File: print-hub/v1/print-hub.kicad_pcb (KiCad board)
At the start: 4 copper layers, 104 x 66 mm, 136 parts, among them J1 USB-C, J101 USB-A, J2 USB-C, J201 USB-A, J301 USB-A, J401 USB-A, J501 USB-A, SW1 button, SW2 button, U1 HUSB238, U101 TPS25200, U102 INA180A2, U2 SY8368A, U201 TPS25200, U202 INA180A2, U3 USBLC6-2SC6, U301 TPS25200, U302 INA180A2, U4 AP2112K-3.3, U401 TPS25200, U402 INA180A2, U5 ESP32-S3-WROOM-1-N8, U501 TPS25200, U502 INA180A2

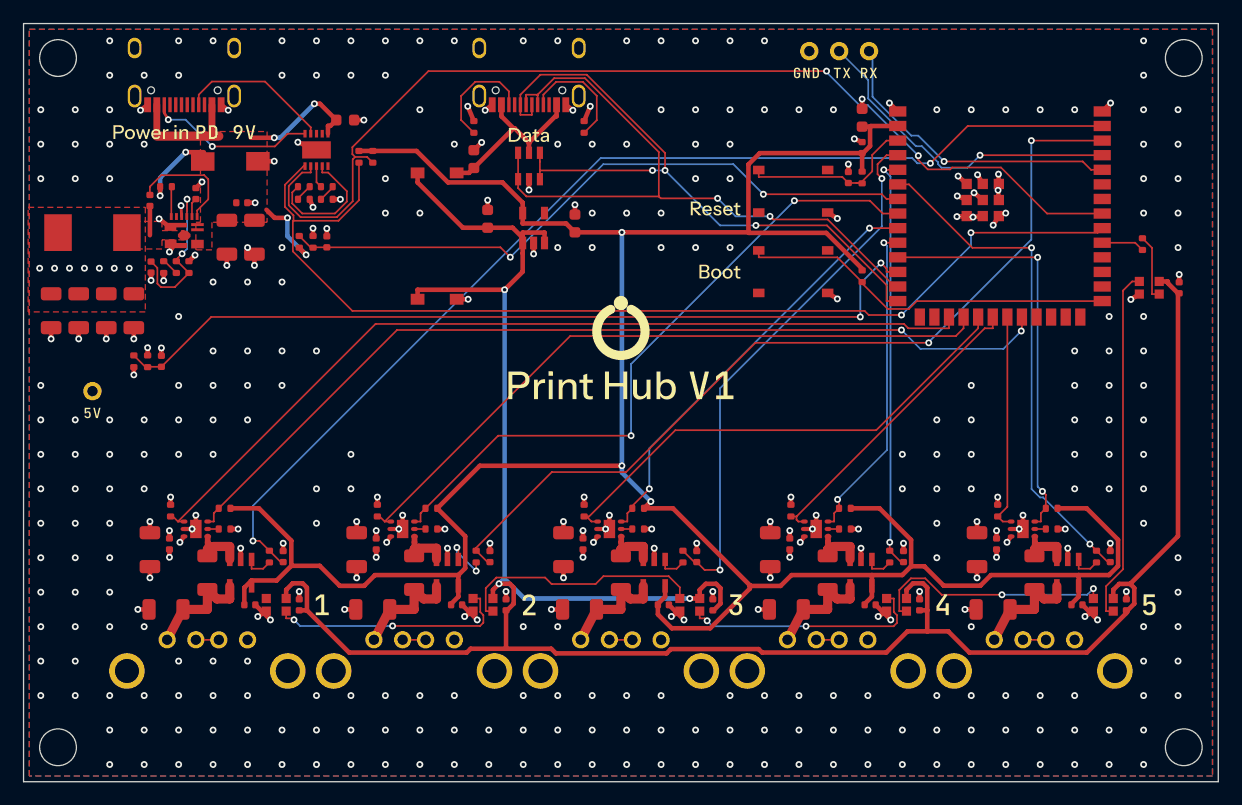
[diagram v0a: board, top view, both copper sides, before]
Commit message: print-hub v1: 86 x 50 mm board, 45-degree corners, heat simulation and protection
- Board shrunk from 104 x 66 to 86 x 50 mm (under JLCPCB's 100 mm price
  break: $8 for five 4-layer boards instead of $29); ports 17 mm apart,
  two M3 holes; green mask, lead-free HASL (cheapest build).
- src/miter.py cuts every track corner to 45 degrees after routing; a
  build gate checks it. Port power tracks drawn with 45-degree bends.
- sim/thermal/board_heat.py: the routed board's heat in its PETG case
  (solver from ridge3-lite). Total output capped at 3 A; a thermistor
  (NTC on GPIO9; port 1's enable moves to GPIO21) lets the firmware turn
  ports down when hot.
- Firmware 1.1.0: heat protection, 3 A budget, 80 MHz CPU; CLI and web
  page show the board temperature. docs/home-assistant.md.
- Enclosure update to follow.

Co-Authored-By: Claude Opus 5.5 <noreply@anthropic.com>
Claude-Session: https://claude.ai/code/session_01AiCo3BFL3vgJ9qSJmY4RFn
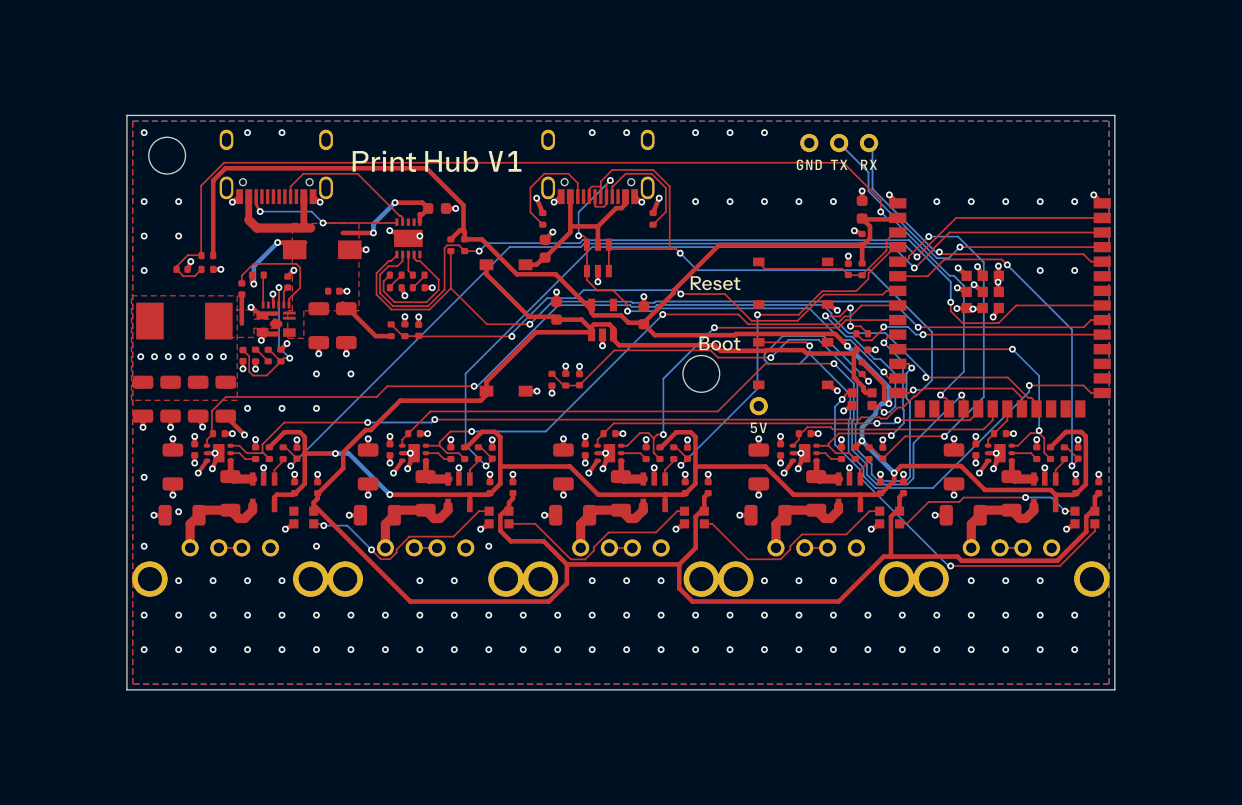
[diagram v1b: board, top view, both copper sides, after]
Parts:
- removed the C11 at (57.6, 92.0)
- removed H3, H4: HOLE, MOUNT_M3
- removed the R10 at (62.4, 88.2)
- added C21: 100nF, C_0402_1005Metric, F.Cu at (121.0, 95.4)
- added C7: 100nF, C_0402_1005Metric, F.Cu at (61.8, 88.4)
- added R12: 10k, R_0402_1005Metric, F.Cu at (70.4, 95.9)
- added R20: 10k, R_0402_1005Metric, F.Cu at (121.0, 97.0)
- added R21: 100R, R_0402_1005Metric, F.Cu at (121.0, 94.0)
- C11: renamed from R12; value 15k -> 22uF; footprint R_0402_1005Metric -> C_1206_3216Metric
- C12: value 100nF -> 22uF; footprint C_0402_1005Metric -> C_1206_3216Metric
- C14: value 10uF -> 100nF; footprint C_0603_1608Metric -> C_0402_1005Metric
- C17: value 22uF -> 10uF
- C18: value 100nF -> 22uF; footprint C_0402_1005Metric -> C_0603_1608Metric
- C19: value 1uF -> 100nF
- C20: value 100nF -> 1uF
- C8: value 22uF -> 22pF; footprint C_1206_3216Metric -> C_0402_1005Metric
- R10: renamed from C7; value 22pF -> 75k; footprint C_0402_1005Metric -> R_0402_1005Metric
- R11: value 100k -> 1k
- R14: value 100k -> 15k
- R15, R16: value 5.1k -> 100k
- R17, R18: value 10k -> 5.1k
- R19: value 100R -> 10k
- R8: value 75k -> 10k NTC
- R9: value 1k -> 10k
- moved TP4 58.0 mm to (112.0, 100.3)
- moved H2 50.2 mm to (107.0, 97.5)
- moved C20 28.8 mm to (119.8, 88.4)
- moved R18 28.2 mm to (93.2, 84.0)
- moved LED1 26.8 mm to (121.0, 99.7)
- moved C17 25.6 mm to (102.0, 92.4)
- moved R19 24.5 mm to (121.0, 88.4)
- moved R16 23.4 mm to (95.2, 98.0)
- moved C13 22.6 mm to (82.4, 93.7)
- moved R14 22.6 mm to (81.2, 93.7)
- moved R13 22.6 mm to (80.0, 93.7)
- moved R15 22.2 mm to (94.0, 98.0)
- moved C14 21.3 mm to (96.4, 98.0)
- moved R17 18.6 mm to (102.8, 84.0)
- moved C8 17.1 mm to (67.1, 95.9), turned to 90 degrees
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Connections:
- C11 pad 1: VIN_SENSE -> VRAIL
- C12 pad 1: VIN_SENSE -> VRAIL
- C13 pad 1: RAIL_SENSE -> VIN_SENSE
- C14 pad 1: VBUS_DATA -> RAIL_SENSE
- C15 pad 1: VLOGIC -> VBUS_DATA
- C16 pad 1: +3V3 -> VLOGIC
- C19 pad 1: ESP_EN -> +3V3
- C20 pad 1: VLOGIC -> ESP_EN
- C8 pad 2: GND -> BUCK_FB
- R10 pad 2: BUCK_FB -> BUCK_FB2
- R11 pad 1: VBUS_IN -> BUCK_FB2
- R11 pad 2: VIN_SENSE -> BUCK_FB
- R13 pad 1: VRAIL -> VBUS_IN
- R13 pad 2: RAIL_SENSE -> VIN_SENSE
- R14 pad 1: RAIL_SENSE -> VIN_SENSE
- R15 pad 1: CC1_DATA -> VRAIL
- R15 pad 2: GND -> RAIL_SENSE
- R16 pad 1: CC2_DATA -> RAIL_SENSE
- R17 pad 1: ESP_EN -> CC1_DATA
- R17 pad 2: +3V3 -> GND
- R18 pad 1: BOOT -> CC2_DATA
- R18 pad 2: +3V3 -> GND
- R19 pad 1: LED_DIN0 -> ESP_EN
- R19 pad 2: LED_D0 -> +3V3
- R8 pad 1: VRAIL -> NTC
- R8 pad 2: BUCK_FB2 -> GND
- R9 pad 1: BUCK_FB2 -> NTC
- R9 pad 2: BUCK_FB -> +3V3
- U5 pad 17: EN1 -> NTC
- U5 pad 23: (no net) -> EN1
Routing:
- net NTC: track 0.00 -> 95.8 mm, vias 0 -> 2
- net VLOGIC: track 210.3 -> 181.9 mm, vias 3 -> 0
- net BOOT: track 32.7 -> 60.6 mm, vias 0 -> 3
- net SDA: track 94.8 -> 75.4 mm
- net LED_DIN0: track 3.76 -> 22.5 mm, vias 0 -> 2
- net RAIL_SENSE: track 73.1 -> 54.5 mm
- net EN5: track 19.1 -> 3.89 mm
- net USB_DN: track 60.1 -> 45.7 mm, vias 2 -> 4
- net IS3: track 47.3 -> 33.2 mm
- net LED_D0: track 5.83 -> 19.4 mm, vias 0 -> 4
- net SCL: track 91.4 -> 78.0 mm
- net FLT5: track 36.2 -> 23.8 mm
- net IS5: track 44.4 -> 32.6 mm
- net IS1: track 94.4 -> 83.0 mm
- net VIN_SENSE: track 57.7 -> 48.6 mm
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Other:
- board size 104 x 66 mm -> 86 x 50 mm
